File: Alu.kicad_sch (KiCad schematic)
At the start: 17 parts, among them U20 Am2920, U21 Am2920, U22 74LS153, U23 74LS153, U24 Am2918, U25 Am2922, U26 Am2903, U27 Am2903, U28 Am2903, U29 Am2903, U30 Am2902A, U33 Am2922, U34 Am2922, U35 Am2922, U36 Am2922, U38 74LS157

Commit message: Schematic complete wrt original
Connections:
- net D0: now also U21.3 (D0)
- net D1: now also U21.4 (D1)
- net D2: now also U21.7 (D2)
- net D3: now also U21.8 (D3)
- net QL: now also U29.1 (QIO0)
- net SL: now also U29.20 (SIO0)
- net carry: now also U23.6 (I0a), U24.2 (Q0), U25.1 (D0)
- net z: now also R2.2, U26.22 (Z), U27.22 (Z), U28.22 (Z), U29.22 (Z)
- net at U23.10 (I0b), U23.11 (I1b), U24.5 (Q1)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: now also U33.13 (D5), U34.13 (D5), U35.13 (D5), U36.13 (D5)
- net at U22.5 (I1a), U22.6 (I0a), U24.11 (Q2)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: now also U33.14 (D4), U34.14 (D4), U35.14 (D4), U36.14 (D4)
- net D12: now reaches U20.13 (D4)
- net D13: now reaches U20.14 (D5)
- net D14: now reaches U20.17 (D6)
- net D15: now reaches U20.18 (D7)
- net D8: now reaches U20.3 (D0)
- net D9: now reaches U20.4 (D1)
- net D10: now reaches U20.7 (D2)
- net D11: now reaches U20.8 (D3)
- net D4: now reaches U21.13 (D4)
- net D5: now reaches U21.14 (D5)
- net D6: now reaches U21.17 (D6)
- net D7: now reaches U21.18 (D7)
- net pl renamed pl38
- net pl35 renamed µ35
- no-connect marks 27 -> 28
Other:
- note added: "Missing # in original"
- note added: "Original was pl35"
- note removed: "ERROR -> missing"
- moved on the sheet: U30, U33, U38

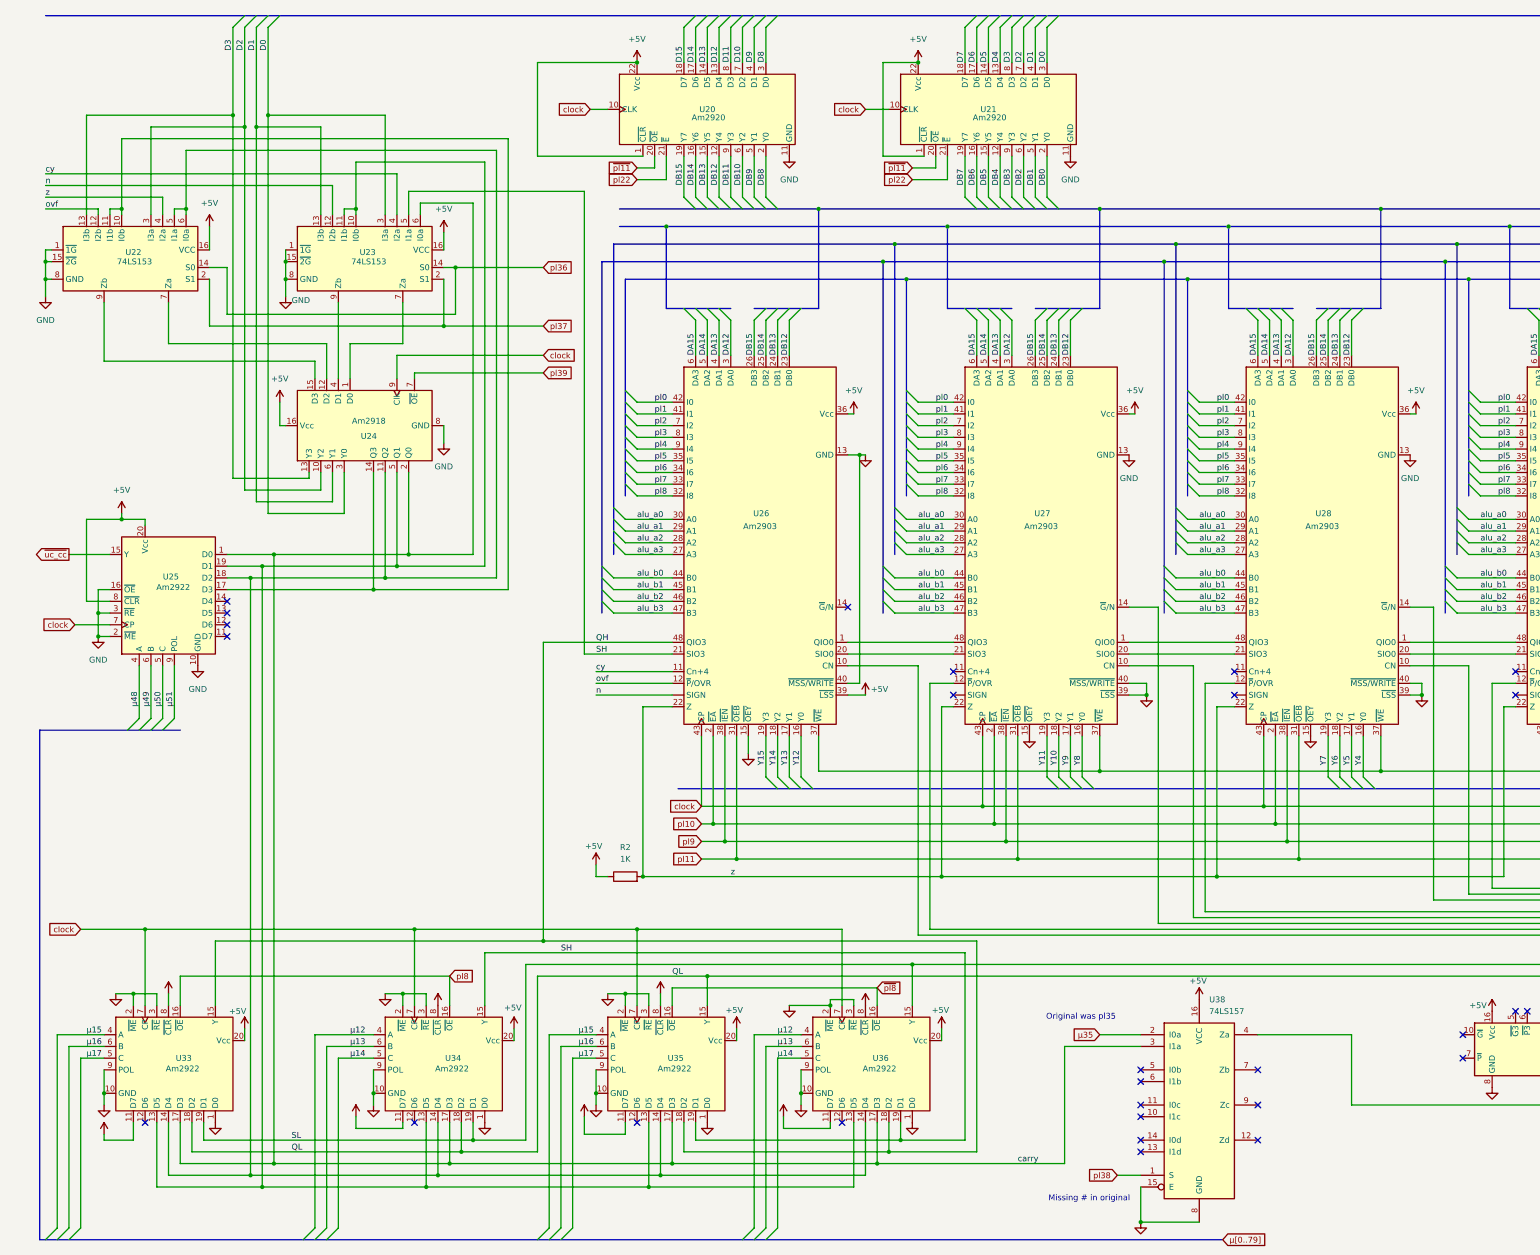
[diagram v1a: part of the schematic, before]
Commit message: Annotate a lot of the schematic with functional descs
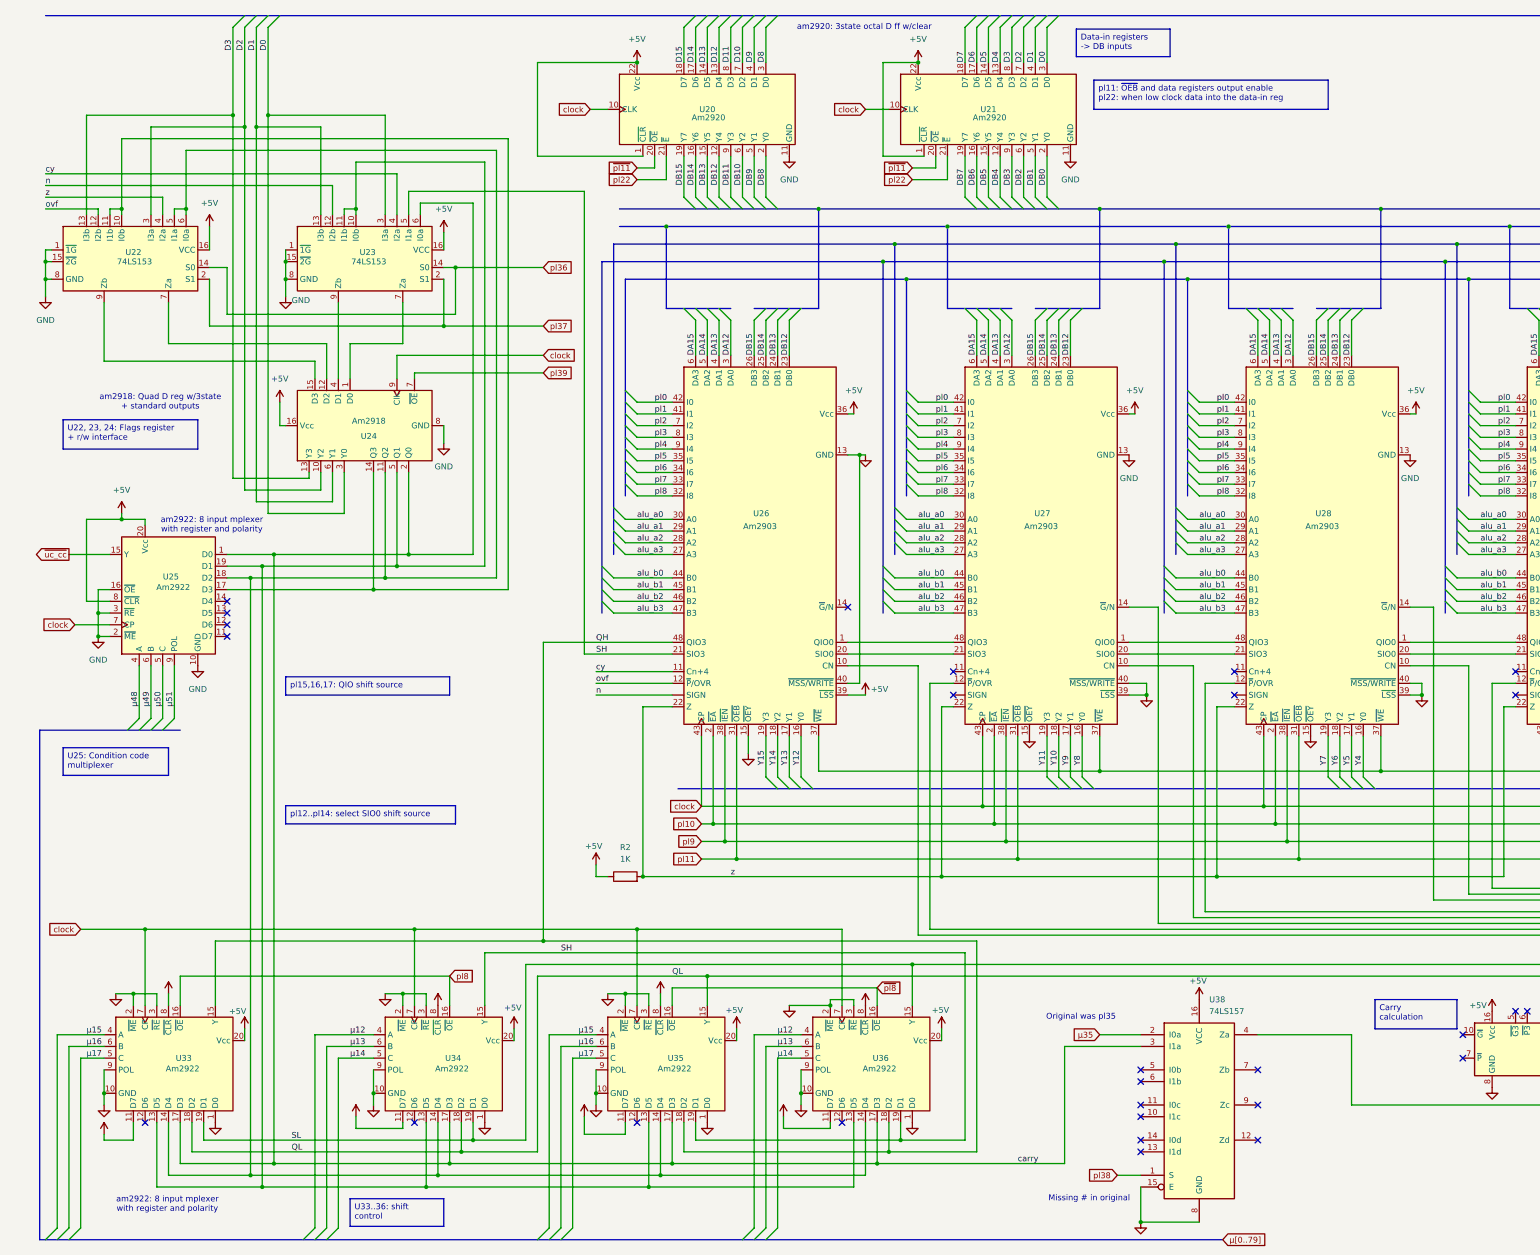
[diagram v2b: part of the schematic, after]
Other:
- note added: "am2918: Quad D reg w/3state + standard outputs"
- note added: "am2920: 3state octal D ff w/clear"
- note added: "am2922: 8 input mplexer with register and polarity"
